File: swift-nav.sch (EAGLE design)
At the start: 172 parts, among them J1 SMA_EDGE, J6 ZX62-B-5PA, Q1 MOSFET-PCHANNELSMD, U1 6SLX9FTG256, U10 MAX2769, U12 PT7M8206B33TA5EX, U13 M25PX80, U2 LTC3407A_DFN, U3 STM32-M-64-LQFP, U4 7Q-16.368MBG-T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

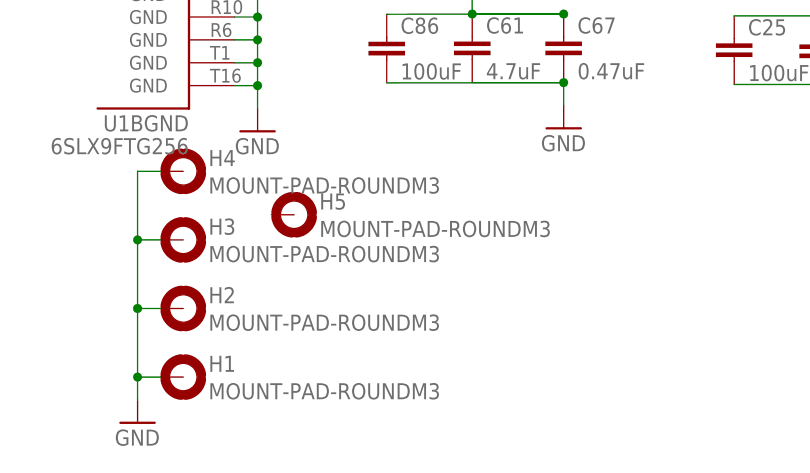
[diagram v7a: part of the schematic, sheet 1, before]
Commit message: Removed extra mounting hole. Still need to move mounting holes in
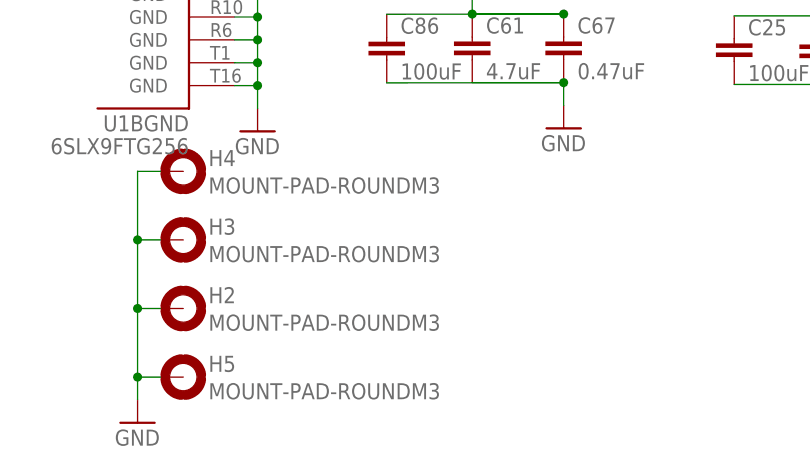
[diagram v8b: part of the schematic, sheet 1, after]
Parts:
- removed H1: MOUNT-PAD-ROUNDM3, swift-nav:MOUNT-PAD-ROUNDM3
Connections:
- net GND: now also H5.MOUNT; no longer H1.MOUNT
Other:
- moved on the sheet: H5
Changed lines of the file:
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@@
 <part name="VCC8" library="supply1" deviceset="VCCIO" device=""/>
 <part name="GND54" library="supply1" deviceset="GND" device=""/>
-<part name="H1" library="swift-nav" deviceset="MOUNT-PAD-ROUND" device="M3"/>
 <part name="GND8" library="supply1" deviceset="GND" device=""/>
 <part name="H2" library="swift-nav" deviceset="MOUNT-PAD-ROUND" device="M3"/>
@@
 <instance part="GND78" gate="1" x="192.151" y="133.35"/>
 <instance part="X2" gate="G$1" x="486.41" y="358.14"/>
-<instance part="H1" gate="G$1" x="38.1" y="15.24"/>
 <instance part="GND8" gate="1" x="33.02" y="10.16"/>
 <instance part="H2" gate="G$1" x="38.1" y="22.86"/>
@@
 <attribute name="VALUE" x="292.608" y="154.051" size="1.778" layer="96" rot="R90"/>
 </instance>
-<instance part="H5" gate="G$1" x="50.419" y="33.274"/>
+<instance part="H5" gate="G$1" x="38.1" y="15.24"/>
 <instance part="VDD1" gate="G$1" x="122.174" y="212.598"/>
 <instance part="VDD2" gate="G$1" x="421.005" y="174.752"/>
@@
 </segment>
 <segment>
-<pinref part="H1" gate="G$1" pin="MOUNT"/>
 <pinref part="GND8" gate="1" pin="GND"/>
 <wire x1="35.56" y1="15.24" x2="33.02" y2="15.24" width="0.1524" layer="91"/>
@@
 <wire x1="35.56" y1="30.48" x2="33.02" y2="30.48" width="0.1524" layer="91"/>
 <junction x="33.02" y="30.48"/>
-</segment>
-<segment>
+<pinref part="H5" gate="G$1" pin="MOUNT"/>
+</segment>
+<segment>
